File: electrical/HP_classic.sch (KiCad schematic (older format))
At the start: 15 parts, among them J1 USB_B_Micro, J2 JST PH 2mm, J3 2.54mm R/A, U1 MCP73831-2-OT

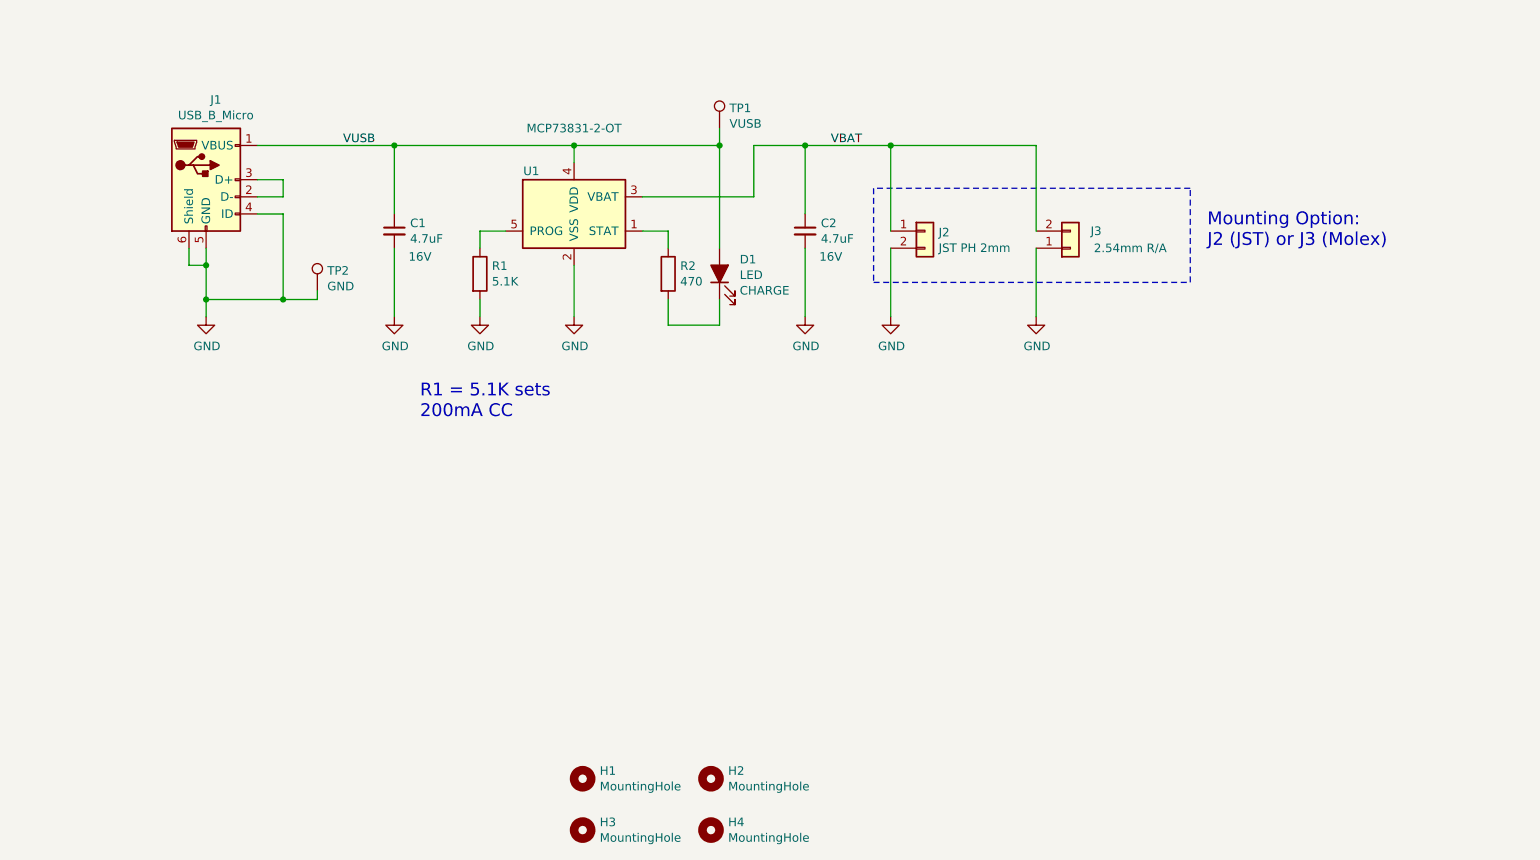
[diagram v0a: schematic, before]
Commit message: upload version 2 ecad and updates
Upload of v2 KiCad schematic, PCB, and BOM information. V2 includes protection circuitry to prevent damage if an HP charger is attached while this pack is installed in the calculator.
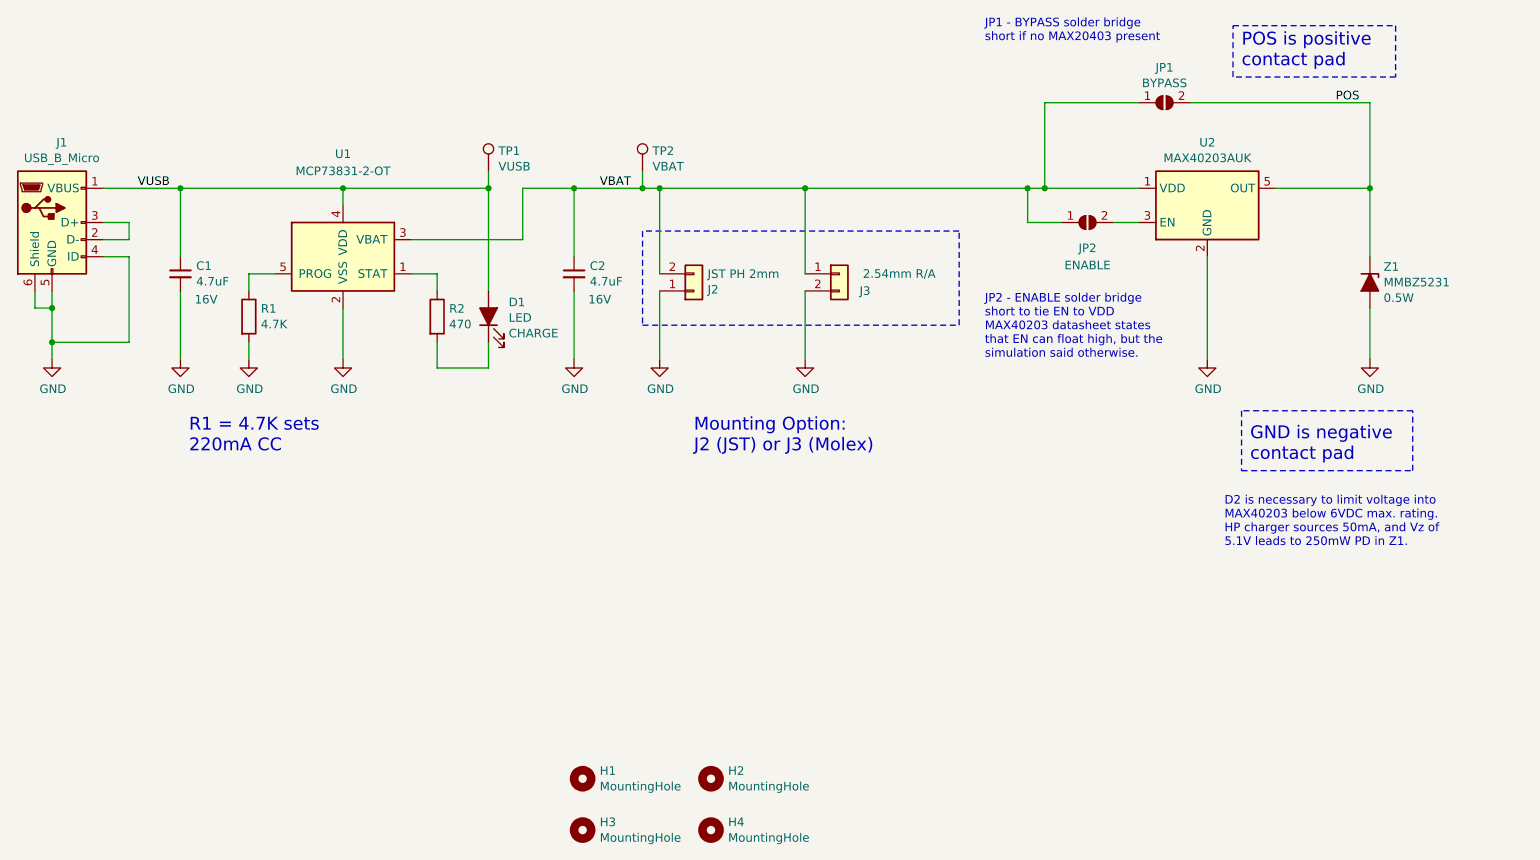
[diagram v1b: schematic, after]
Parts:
- added JP1: BYPASS, Jumper:SolderJumper-2_P1.3mm_Open_RoundedPad1.0x1.5mm, symbol Jumper:SolderJumper_2_Open
- added JP2: ENABLE, Jumper:SolderJumper-2_P1.3mm_Open_RoundedPad1.0x1.5mm, symbol Jumper:SolderJumper_2_Open
- added U2: MAX40203AUK, Package_TO_SOT_SMD:SOT-23-5, symbol Analog_Switch:MAX40200AUK
- added Z1: MMBZ5231, Diode_SMD:D_SOD-123, symbol Device:D_Zener_ALT
- R1: value 5.1K -> 4.7K
- TP2: value GND -> VBAT
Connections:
- net GND: now also J2.1 (Pin_1), J3.2 (Pin_2), U2.2 (GND), Z1.2 (A); no longer J2.2 (Pin_2), J3.1 (Pin_1), TP2.1
- net VBAT: now also J2.2 (Pin_2), J3.1 (Pin_1), TP2.1, JP1.1 (A), JP2.1 (A), U2.1 (VDD); no longer J2.1 (Pin_1), J3.2 (Pin_2)
- new net: JP2.2 (B), U2.3 (EN)
- new net POS: JP1.2 (B), U2.5 (OUT), Z1.1 (K)
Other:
- note added: "D2 is necessary to limit voltage into\nMAX40203 below 6VDC max. rating.\nHP charger sources 50mA, and Vz of\n5.1V leads to 250mW PD in Z1."
- note added: "GND is negative\ncontact pad"
- note added: "JP1 - BYPASS solder bridge\nshort if no MAX20403 present"
- note added: "JP2 - ENABLE solder bridge\nshort to tie EN to VDD\nMAX40203 datasheet states\nthat EN can float high, but the\nsimulation said otherwise."
- note added: "POS is positive \ncontact pad"
- note added: "R1 = 4.7K sets\n220mA CC"
- note removed: "R1 = 5.1K sets\n200mA CC"
- moved on the sheet: C1, C2, D1, J1, J2, J3, R1, R2, TP1, TP2, U1
